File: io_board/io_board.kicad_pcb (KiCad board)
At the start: 2 copper layers, 80 x 100 mm, 89 parts, among them J10 RST1, J11 D1, J12 Osc2, J13 Rung2, J14 Sin2, J15 Gate2, J16 Ring, J18 RST2, J19 D2, J21 CV1, J22 CV2, J4 STRB1, J5 STRB2, J6 Osc1, J7 Sin1, J8 Rung1, J9 Gate1, Q1 2N3904, Q10 2N3904, Q11 2N3904, Q2 2N3904, Q5 2N3904, Q6 2N3904, Q7 2N3904, Q8 2N3904, Q9 2N3904, SW1 SW_SPDT, U3 TL074

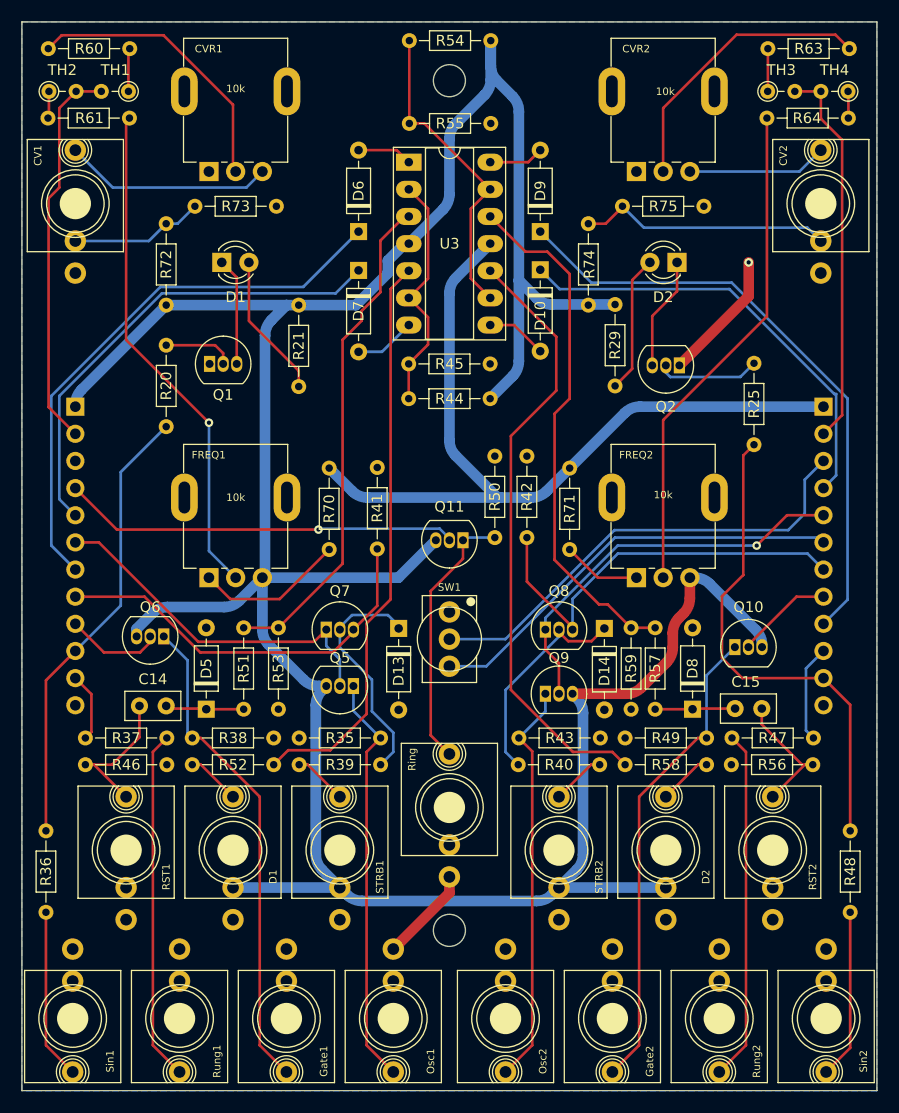
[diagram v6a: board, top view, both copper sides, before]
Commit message: Added range switch
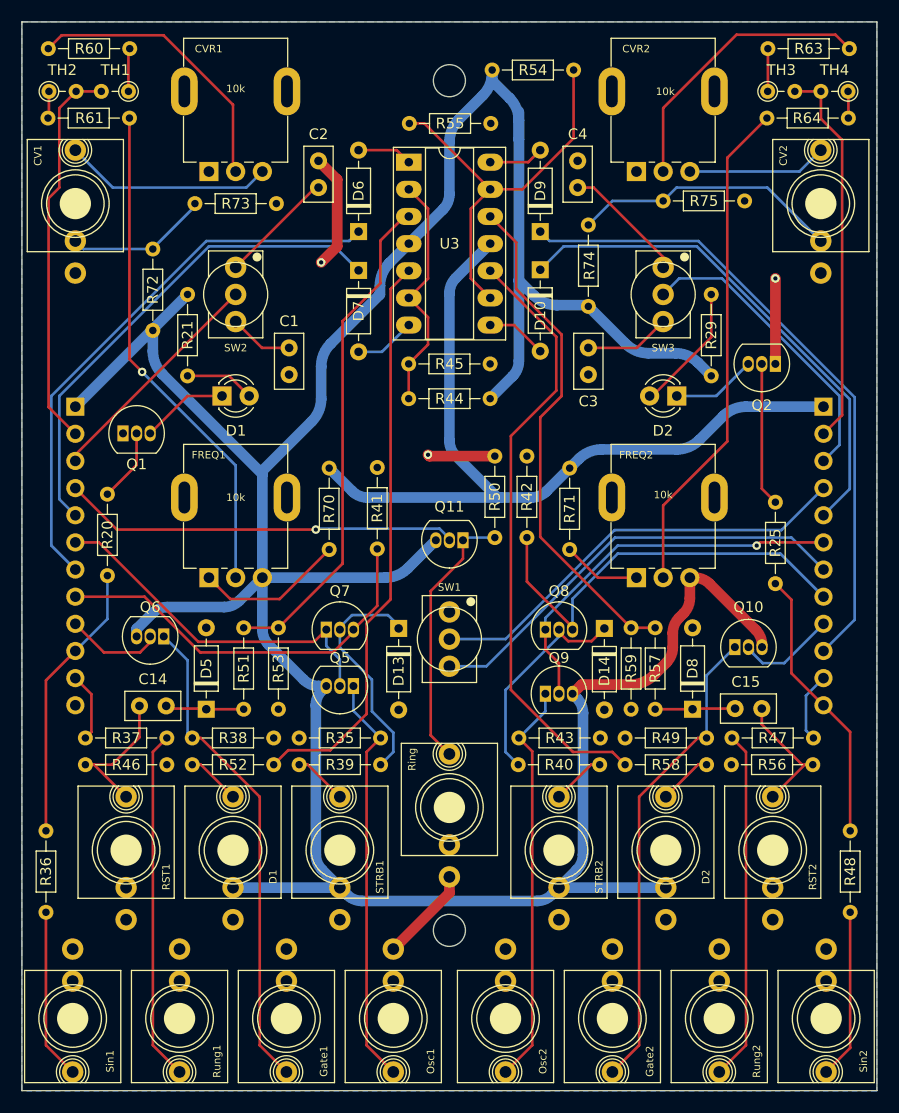
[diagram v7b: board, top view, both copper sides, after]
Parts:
- added C1: 1nF, Capacitor_THT:C_Disc_D5.0mm_W2.5mm_P2.50mm, F.Cu at (25.0, 30.5)
- added C2: 100nF, Capacitor_THT:C_Disc_D5.0mm_W2.5mm_P2.50mm, F.Cu at (27.8, 15.5)
- added C3: 1nF, Capacitor_THT:C_Disc_D5.0mm_W2.5mm_P2.50mm, F.Cu at (53.0, 30.5)
- added C4: 100nF, Capacitor_THT:C_Disc_D5.0mm_W2.5mm_P2.50mm, F.Cu at (52.0, 15.5)
- added SW2: SW_SPDT, winterbloom:Miniature_Switch_SPDT_2.54MM, F.Cu at (20.0, 25.5)
- added SW3: SW_SPDT, winterbloom:Miniature_Switch_SPDT_2.54MM, F.Cu at (60.0, 25.5)
- moved R20 15.0 mm to (8.00, 44.2)
- moved R25 13.2 mm to (70.5, 44.9)
- moved D1 12.5 mm to (18.7, 35.0)
- moved D2 12.5 mm to (61.3, 35.0)
- moved R29 11.2 mm to (64.5, 33.1), turned to 90 degrees
- moved R21 10.4 mm to (15.5, 25.5)
- moved Q1 10.4 mm to (9.46, 38.5)
- moved Q2 8.98 mm to (70.5, 32.0)
- moved R75 3.84 mm to (60.0, 16.8)
- moved R54 2.75 mm to (44.0, 4.50), turned to 0 degrees
- moved R72 2.68 mm to (12.2, 28.9)
- moved R73 0.25 mm to (16.2, 17.0)
- moved R74 0.12 mm to (53.0, 26.6)
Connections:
- J17 pad 3: unconnected-(J17-Pad3) -> RATESEL1
- J20 pad 10: Rung2 -> Rst2
- J20 pad 11: Sin2 -> Rung2
- J20 pad 12: GND -> Sin2
- J20 pad 3: Osc3sw -> RATESEL2
- J20 pad 4: D2 -> Osc3sw
- J20 pad 5: Osc2 -> D2
- J20 pad 6: Osc3 -> Osc2
- J20 pad 7: Clk2 -> Osc3
- J20 pad 8: QB8 -> Clk2
- J20 pad 9: Rst2 -> QB8
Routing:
- net RATESEL2: track 0.00 -> 28.4 mm
- net RATESEL1: track 0.00 -> 21.8 mm
- net Sin2: track 46.8 -> 26.0 mm
- net Sin1: track 42.5 -> 26.3 mm
- net GND: track 21.2 -> 34.1 mm, vias 1 -> 3
- net 12v: track 286.4 -> 298.6 mm
- net Net-(C4-Pad1): track 0.00 -> 11.7 mm
- net Net-(C2-Pad1): track 0.00 -> 10.8 mm
- net Net-(R54-Pad2): track 29.5 -> 38.0 mm
- net Net-(C3-Pad1): track 0.00 -> 8.02 mm
- net Net-(D1-Pad2): track 13.6 -> 6.54 mm
- net Net-(C1-Pad1): track 0.00 -> 6.02 mm
- net D2: track 41.8 -> 47.7 mm
- net Net-(Q2-Pad2): track 9.63 -> 13.5 mm
- net Rst2: track 57.2 -> 60.8 mm
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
